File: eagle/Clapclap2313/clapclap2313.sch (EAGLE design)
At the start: 20 parts, among them K1 4052, M1 Mic

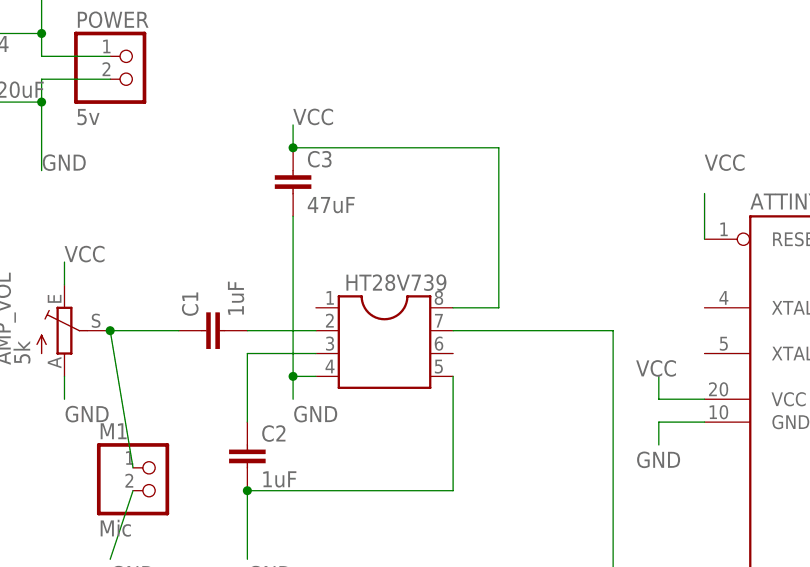
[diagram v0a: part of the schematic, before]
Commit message: Thanks to Mr. Girts from Riga, the name of the amp is now fixed.
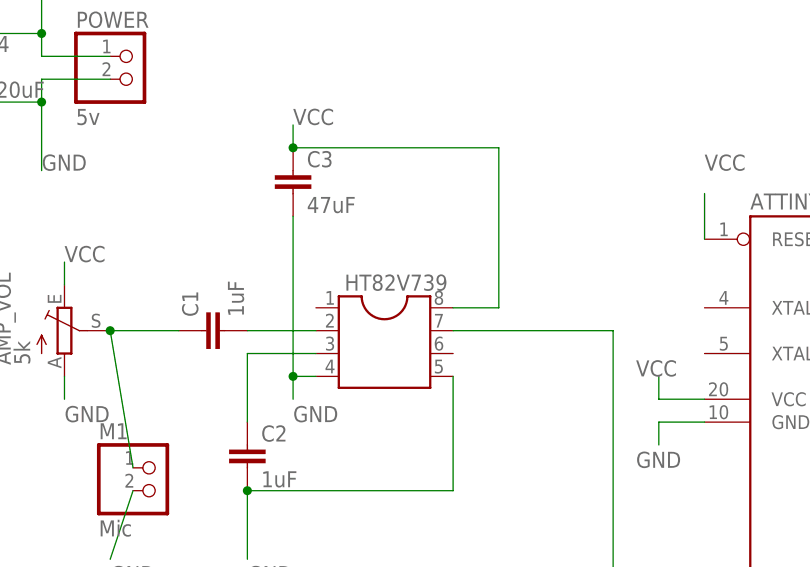
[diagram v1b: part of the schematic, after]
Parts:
- renumbered HT28V739 to HT82V739
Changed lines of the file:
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@@
 <parts>
 <part name="ATTINY2313" library="atmel" deviceset="AT90S2313" device="P"/>
-<part name="HT28V739" library="ic-package" deviceset="DIL8" device="S"/>
+<part name="HT82V739" library="ic-package" deviceset="DIL8" device="S"/>
 <part name="M1" library="pinhead" deviceset="PINHD-1X2" device="" value="Mic"/>
 <part name="NPN" library="transistor" deviceset="*-NPN-" device="TO92-ECB" value="2SC2120"/>
@@
 <instances>
 <instance part="ATTINY2313" gate="G$1" x="58.42" y="48.26"/>
-<instance part="HT28V739" gate="G$1" x="5.08" y="58.42"/>
+<instance part="HT82V739" gate="G$1" x="5.08" y="58.42"/>
 <instance part="M1" gate="G$1" x="-20.32" y="40.64"/>
 <instance part="NPN" gate="G$1" x="106.68" y="63.5"/>
@@
 <wire x1="-10.16" y1="58.42" x2="-2.54" y2="58.42" width="0.1524" layer="91"/>
 <pinref part="C1" gate="G$1" pin="2"/>
-<pinref part="HT28V739" gate="G$1" pin="2"/>
+<pinref part="HT82V739" gate="G$1" pin="2"/>
 </segment>
 </net>
@@
 <wire x1="83.82" y1="22.86" x2="83.82" y2="50.8" width="0.1524" layer="91"/>
 <wire x1="83.82" y1="50.8" x2="76.2" y2="50.8" width="0.1524" layer="91"/>
-<pinref part="HT28V739" gate="G$1" pin="7"/>
+<pinref part="HT82V739" gate="G$1" pin="7"/>
 <pinref part="ATTINY2313" gate="G$1" pin="(AIN0)PB0"/>
 </segment>
@@
 <label x="-5.08" y="81.28" size="1.778" layer="95"/>
 <pinref part="C3" gate="G$1" pin="1"/>
-<pinref part="HT28V739" gate="G$1" pin="8"/>
+<pinref part="HT82V739" gate="G$1" pin="8"/>
 </segment>
 <segment>
@@
 <junction x="-10.16" y="40.64"/>
 <label x="-10.16" y="30.48" size="1.778" layer="95"/>
-<pinref part="HT28V739" gate="G$1" pin="5"/>
+<pinref part="HT82V739" gate="G$1" pin="5"/>
 <pinref part="C2" gate="G$1" pin="2"/>
 </segment>
@@
 <junction x="-5.08" y="53.34"/>
 <label x="-5.08" y="48.26" size="1.778" layer="95"/>
-<pinref part="HT28V739" gate="G$1" pin="4"/>
+<pinref part="HT82V739" gate="G$1" pin="4"/>
 <pinref part="C3" gate="G$1" pin="2"/>
 </segment>
@@
 <wire x1="-2.54" y1="55.88" x2="-10.16" y2="55.88" width="0.1524" layer="91"/>
 <wire x1="-10.16" y1="55.88" x2="-10.16" y2="48.26" width="0.1524" layer="91"/>
-<pinref part="HT28V739" gate="G$1" pin="3"/>
+<pinref part="HT82V739" gate="G$1" pin="3"/>
 <pinref part="C2" gate="G$1" pin="1"/>
 </segment>

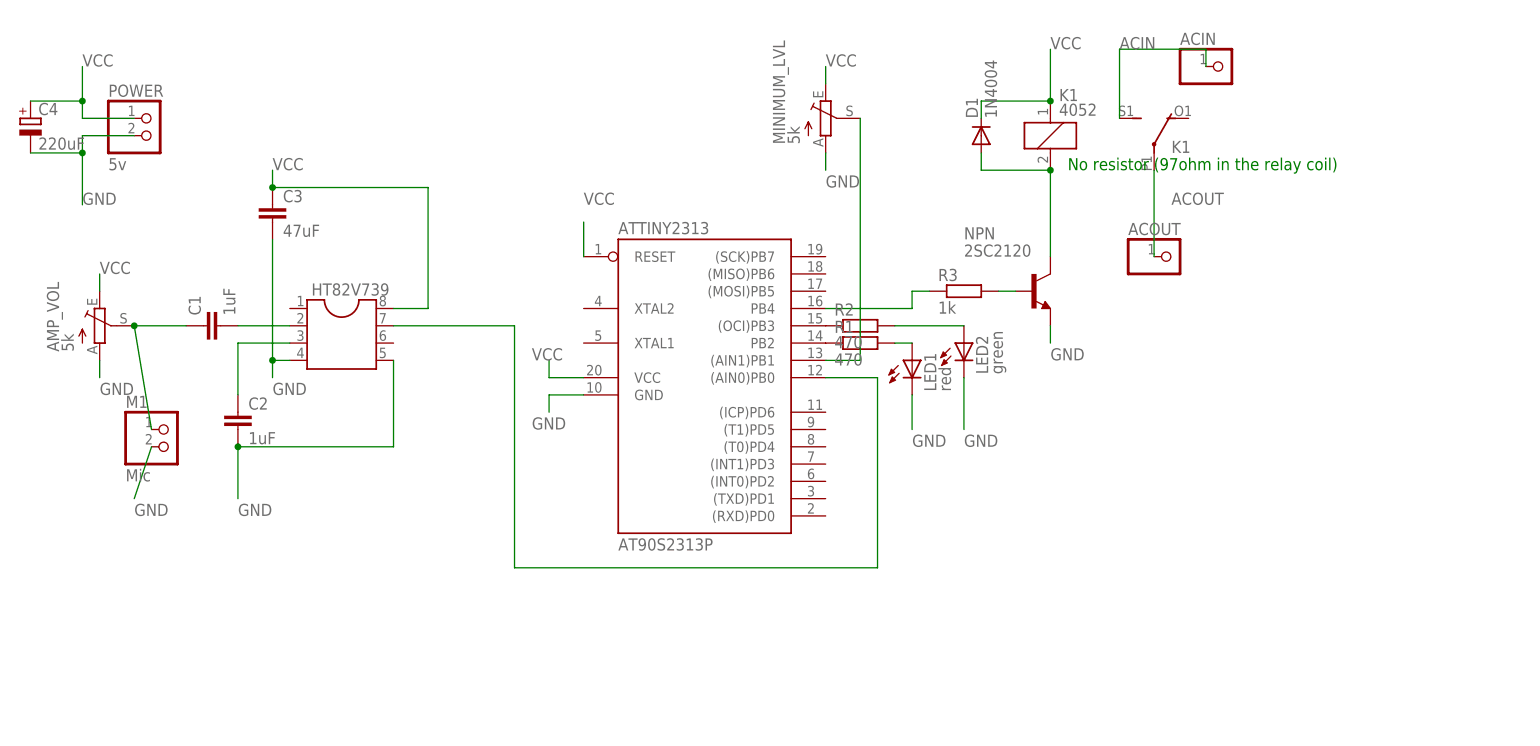
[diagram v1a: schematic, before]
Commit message: v1.2 : before last labels and check. Made a VCC/AC zone, added pins for AC solder, fat traces to handle amps.
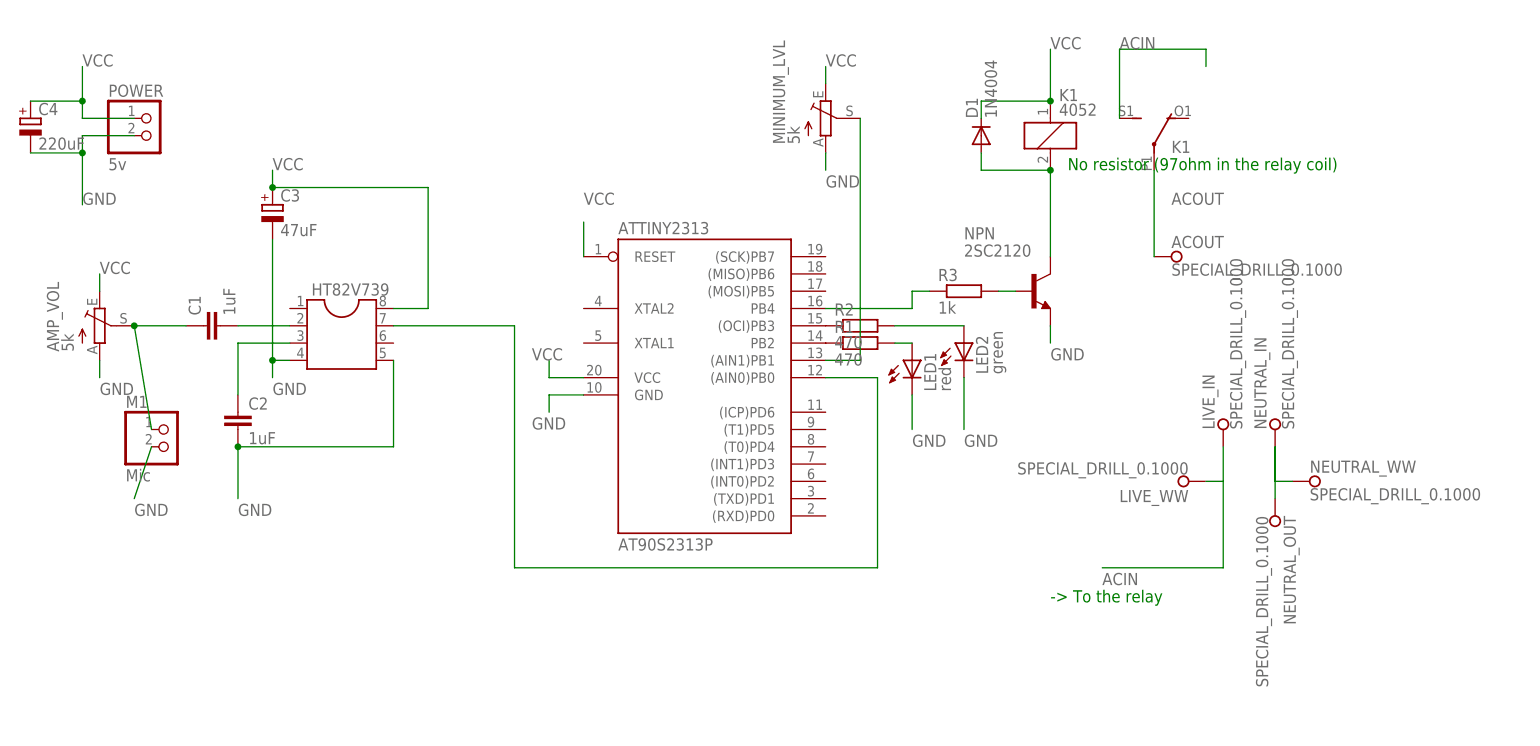
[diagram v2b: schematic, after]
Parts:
- removed ACIN: (no value), pinhead:PINHD-1X1
- added LIVE_IN, LIVE_WW, NEUTRAL_IN, NEUTRAL_OUT, NEUTRAL_WW: SPECIAL_DRILL_0.1000, special-drill:SPECIAL_DRILL_0.1000
- ACOUT: value (none) -> SPECIAL_DRILL_0.1000; device pinhead:PINHD-1X1 -> special-drill:SPECIAL_DRILL_0.1000
- C3: device resistor:C-EU050-024X044 -> resistor:CPOL-EUE2.5-6
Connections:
- new net N$13: NEUTRAL_IN.1, NEUTRAL_OUT.1, NEUTRAL_WW.1
- net ACIN: now also LIVE_IN.1, LIVE_WW.1; no longer ACIN.1
- net GND: now also C3.-; no longer C3.2
- net VCC: now also C3.+; no longer C3.1
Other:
- note added: "-> To the relay"
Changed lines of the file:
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@@
 <part name="C1" library="resistor" deviceset="C-EU" device="050-024X044" value="1uF"/>
 <part name="C2" library="resistor" deviceset="C-EU" device="050-024X044" value="1uF"/>
-<part name="C3" library="resistor" deviceset="C-EU" device="050-024X044" value="47uF"/>
+<part name="C3" library="resistor" deviceset="CPOL-EU" device="E2.5-6" value="47uF"/>
 <part name="R3" library="resistor" deviceset="R-EU_" device="0207/2V" value="1k"/>
 <part name="D1" library="diode" deviceset="1N4004" device=""/>
@@
 <part name="R1" library="resistor" deviceset="R-EU_" device="0204/2V" value="470"/>
 <part name="R2" library="resistor" deviceset="R-EU_" device="0204/2V" value="470"/>
-<part name="ACIN" library="pinhead" deviceset="PINHD-1X1" device=""/>
-<part name="ACOUT" library="pinhead" deviceset="PINHD-1X1" device=""/>
+<part name="ACOUT" library="special-drill" deviceset="SPECIAL_DRILL_" device="0.1000"/>
+<part name="LIVE_IN" library="special-drill" deviceset="SPECIAL_DRILL_" device="0.1000"/>
+<part name="NEUTRAL_IN" library="special-drill" deviceset="SPECIAL_DRILL_" device="0.1000"/>
+<part name="NEUTRAL_OUT" library="special-drill" deviceset="SPECIAL_DRILL_" device="0.1000"/>
+<part name="LIVE_WW" library="special-drill" deviceset="SPECIAL_DRILL_" device="0.1000"/>
+<part name="NEUTRAL_WW" library="special-drill" deviceset="SPECIAL_DRILL_" device="0.1000"/>
 </parts>
 <sheets>
@@
 <plain>
 <text x="111.76" y="81.28" size="1.778" layer="91">No resistor (97ohm in the relay coil)</text>
+<text x="109.22" y="17.78" size="1.778" layer="91">-&gt; To the relay</text>
 </plain>
 <instances>
@@
 <instance part="R1" gate="G$1" x="81.28" y="55.88"/>
 <instance part="R2" gate="G$1" x="81.28" y="58.42"/>
-<instance part="ACIN" gate="G$1" x="134.62" y="96.52"/>
 <instance part="ACOUT" gate="G$1" x="127" y="68.58"/>
+<instance part="LIVE_IN" gate="G$1" x="134.62" y="43.18" rot="R90"/>
+<instance part="NEUTRAL_IN" gate="G$1" x="142.24" y="43.18" rot="R90"/>
+<instance part="NEUTRAL_OUT" gate="G$1" x="142.24" y="30.48" rot="R270"/>
+<instance part="LIVE_WW" gate="G$1" x="129.54" y="35.56" rot="R180"/>
+<instance part="NEUTRAL_WW" gate="G$1" x="147.32" y="35.56"/>
 </instances>
 <busses>
@@
 <junction x="-5.08" y="78.74"/>
 <label x="-5.08" y="81.28" size="1.778" layer="95"/>
-<pinref part="C3" gate="G$1" pin="1"/>
+<pinref part="C3" gate="G$1" pin="+"/>
 <pinref part="HT82V739" gate="G$1" pin="8"/>
 </segment>
@@
 <label x="-5.08" y="48.26" size="1.778" layer="95"/>
 <pinref part="HT82V739" gate="G$1" pin="4"/>
-<pinref part="C3" gate="G$1" pin="2"/>
+<pinref part="C3" gate="G$1" pin="-"/>
 </segment>
 <segment>
@@
 <label x="119.38" y="99.06" size="1.778" layer="95"/>
 <pinref part="K1" gate="2" pin="S"/>
-<pinref part="ACIN" gate="G$1" pin="1"/>
+</segment>
+<segment>
+<pinref part="LIVE_IN" gate="G$1" pin="1"/>
+<wire x1="134.62" y1="40.64" x2="134.62" y2="35.56" width="0.1524" layer="91"/>
+<pinref part="LIVE_WW" gate="G$1" pin="1"/>
+<wire x1="134.62" y1="35.56" x2="132.08" y2="35.56" width="0.1524" layer="91"/>
+<wire x1="134.62" y1="35.56" x2="134.62" y2="22.86" width="0.1524" layer="91"/>
+<wire x1="134.62" y1="22.86" x2="116.84" y2="22.86" width="0.1524" layer="91"/>
+<label x="116.84" y="20.32" size="1.778" layer="95"/>
 </segment>
 </net>
@@
 </segment>
 </net>
+<net name="N$13" class="0">
+<segment>
+<pinref part="NEUTRAL_IN" gate="G$1" pin="1"/>
+<pinref part="NEUTRAL_OUT" gate="G$1" pin="1"/>
+<wire x1="142.24" y1="40.64" x2="142.24" y2="33.02" width="0.1524" layer="91"/>
+<pinref part="NEUTRAL_WW" gate="G$1" pin="1"/>
+<wire x1="144.78" y1="35.56" x2="142.24" y2="35.56" width="0.1524" layer="91"/>
+<wire x1="142.24" y1="35.56" x2="142.24" y2="40.64" width="0.1524" layer="91"/>
+</segment>
+</net>
